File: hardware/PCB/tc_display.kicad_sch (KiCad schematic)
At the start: 41 parts, among them Q1 2N2222, Q2 2N2222, U10 SA15-11SRWA, U11 SA15-11SRWA, U12 SA15-11SRWA, U13 SA15-11SRWA, U14 SA15-11SRWA, U15 SA15-11SRWA, U16 MAX7219, U17 SA15-11SRWA, U18 SA15-11SRWA, U19 SA15-11SRWA, U20 SA15-11SRWA, U3 SA15-11SRWA, U4 SA15-11SRWA, U5 SA15-11SRWA, U6 SA15-11SRWA, U7 MAX7219, U8 SA15-11SRWA, U9 SA15-11SRWA

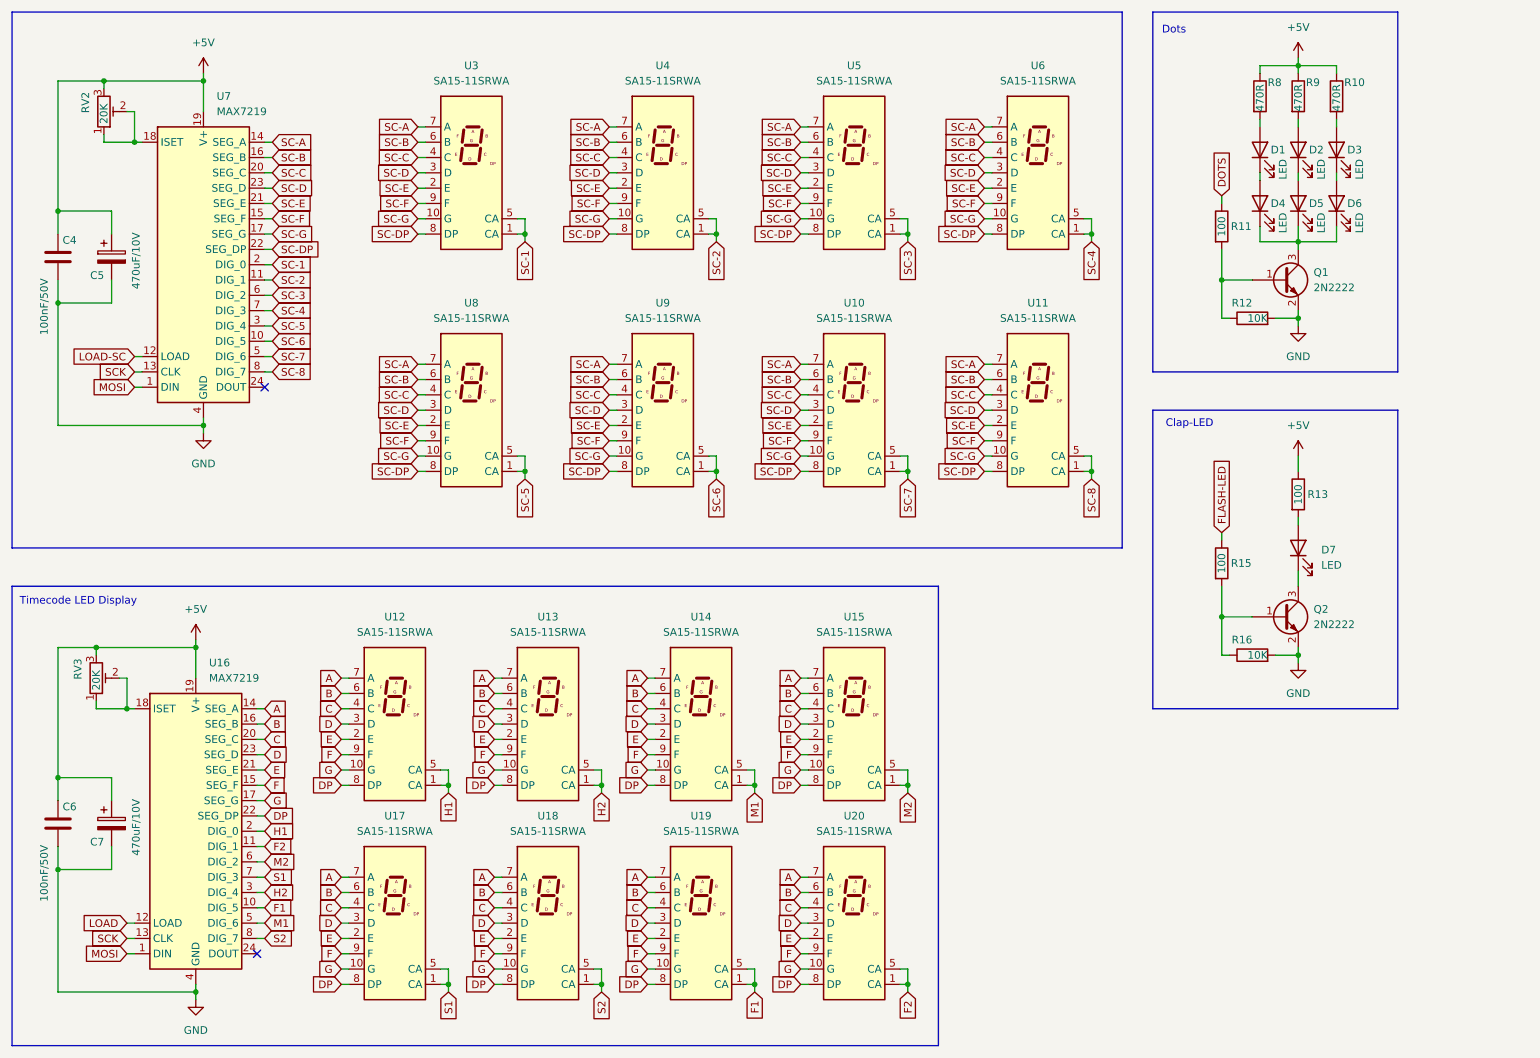
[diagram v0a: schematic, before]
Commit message: dot matrix bugfixes
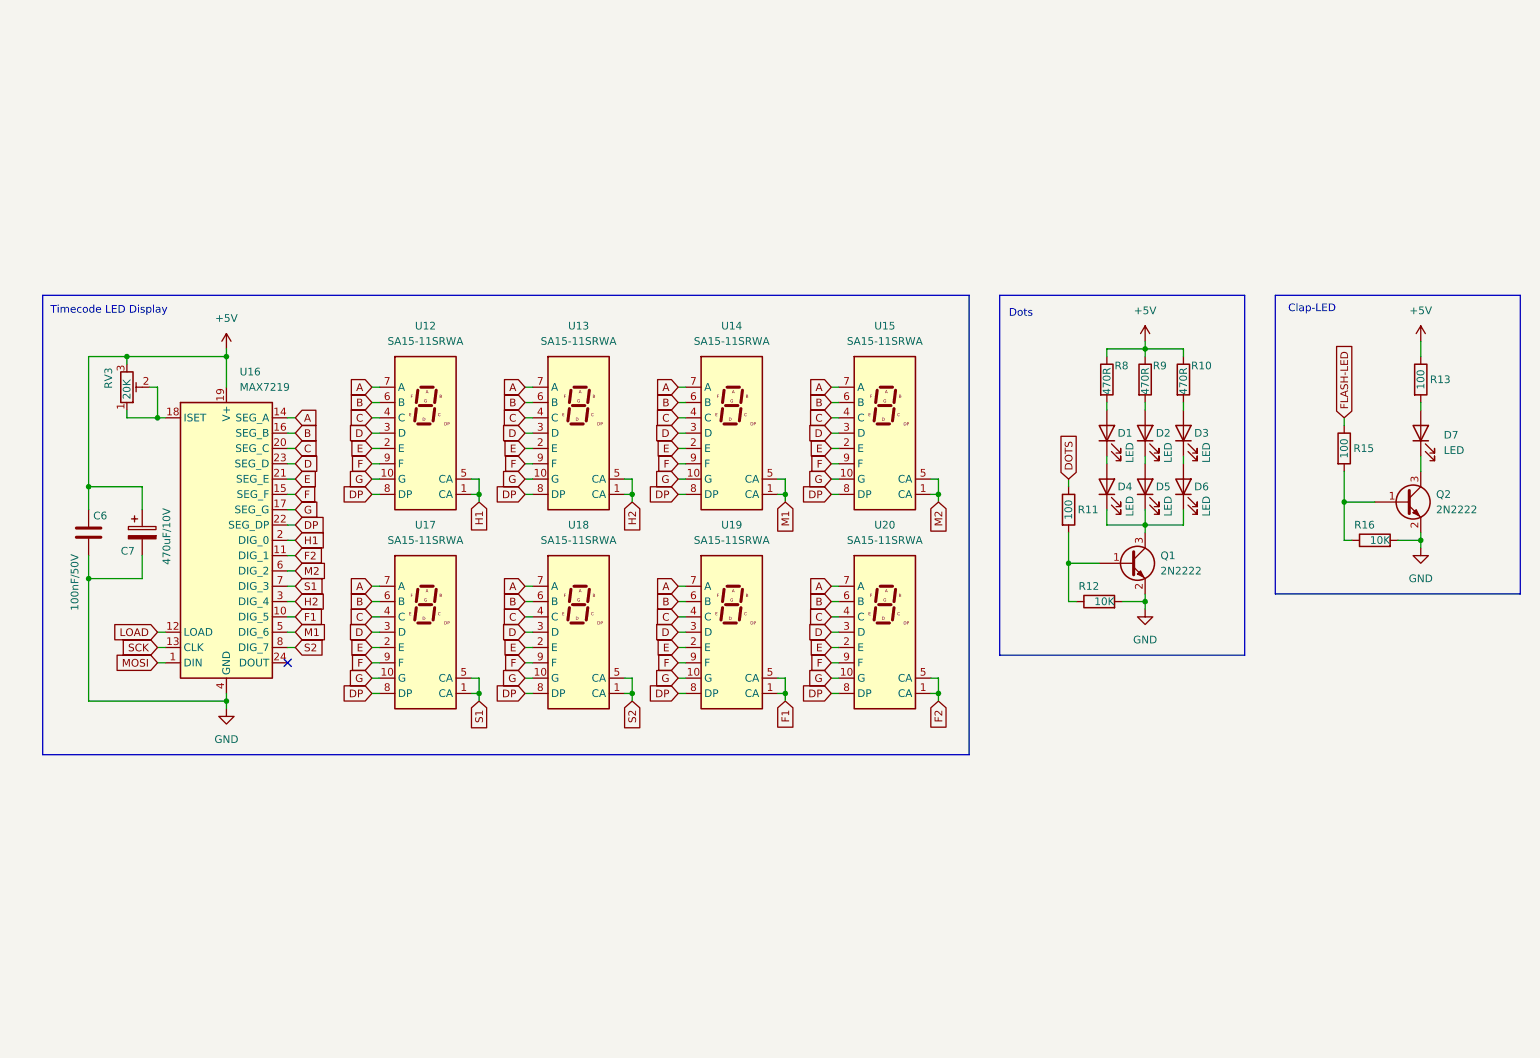
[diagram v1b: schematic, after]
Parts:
- removed C4: 100nF/50V, Capacitor_SMD:C_1206_3216Metric_Pad1.33x1.80mm_HandSolder, symbol Device:C
- removed C5: 470uF/10V, Capacitor_Tantalum_SMD:CP_EIA-7343-31_Kemet-D_Pad2.25x2.55mm_HandSolder, symbol Device:C_Polarized
- removed RV2: 20K, Potentiometer_SMD:Potentiometer_Vishay_TS53YL_Vertical, symbol Device:R_Potentiometer_Trim
- removed U10, U11, U3, U4, U5, U6, U8, U9: SA15-11SRWA, 7-segment-led:FYS-12011A, symbol Display_Character:SA15-11SRWA
- removed U7: MAX7219, Package_SO:SOIC-24W_7.5x15.4mm_P1.27mm, symbol Driver_LED:MAX7219
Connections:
- no-connect marks 2 -> 1
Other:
- moved on the sheet: C6, C7, D1, D2, D3, D4, D5, D6, D7, Q1, Q2, R10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

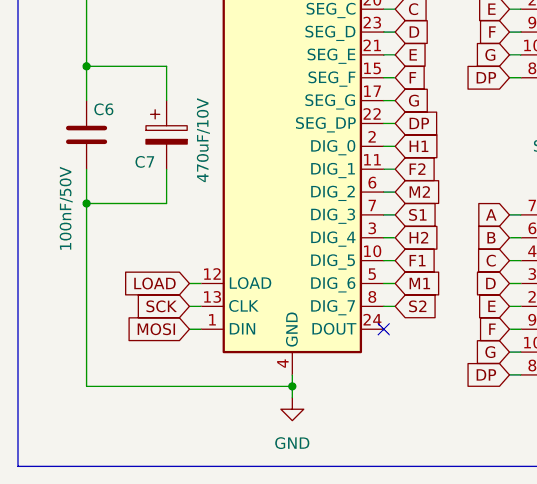
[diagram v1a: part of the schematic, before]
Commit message: added KiCad libraries schematic bugfixes
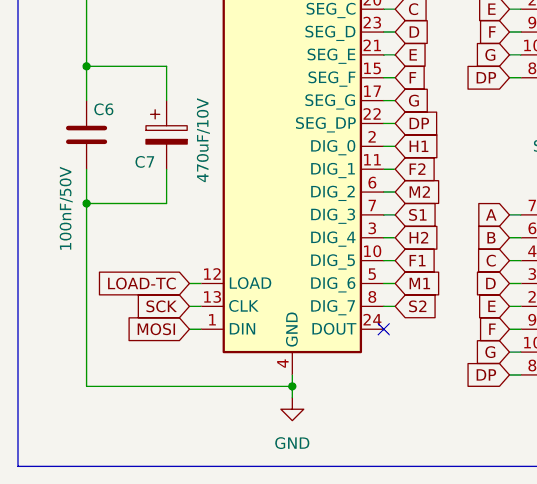
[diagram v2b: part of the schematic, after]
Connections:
- net LOAD renamed LOAD-TC
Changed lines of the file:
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@@
 		)
 	)
-	(global_label "LOAD"
+	(global_label "LOAD-TC"
 		(shape input)
 		(at 44.45 120.65 180)
@@
 		)
 		(property "Intersheetrefs" "${INTERSHEET_REFS}"
-			(at 36.7476 120.65 0)
+			(at 32.9376 120.65 0)
 			(effects
 				(font

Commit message: KiCAD bagfix update
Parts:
- R11: value 100 -> 1k5
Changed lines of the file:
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@@
 			)
 		)
-		(property "Value" "100"
+		(property "Value" "1k5"
 			(at 195.58 100.33 90)
 			(effects

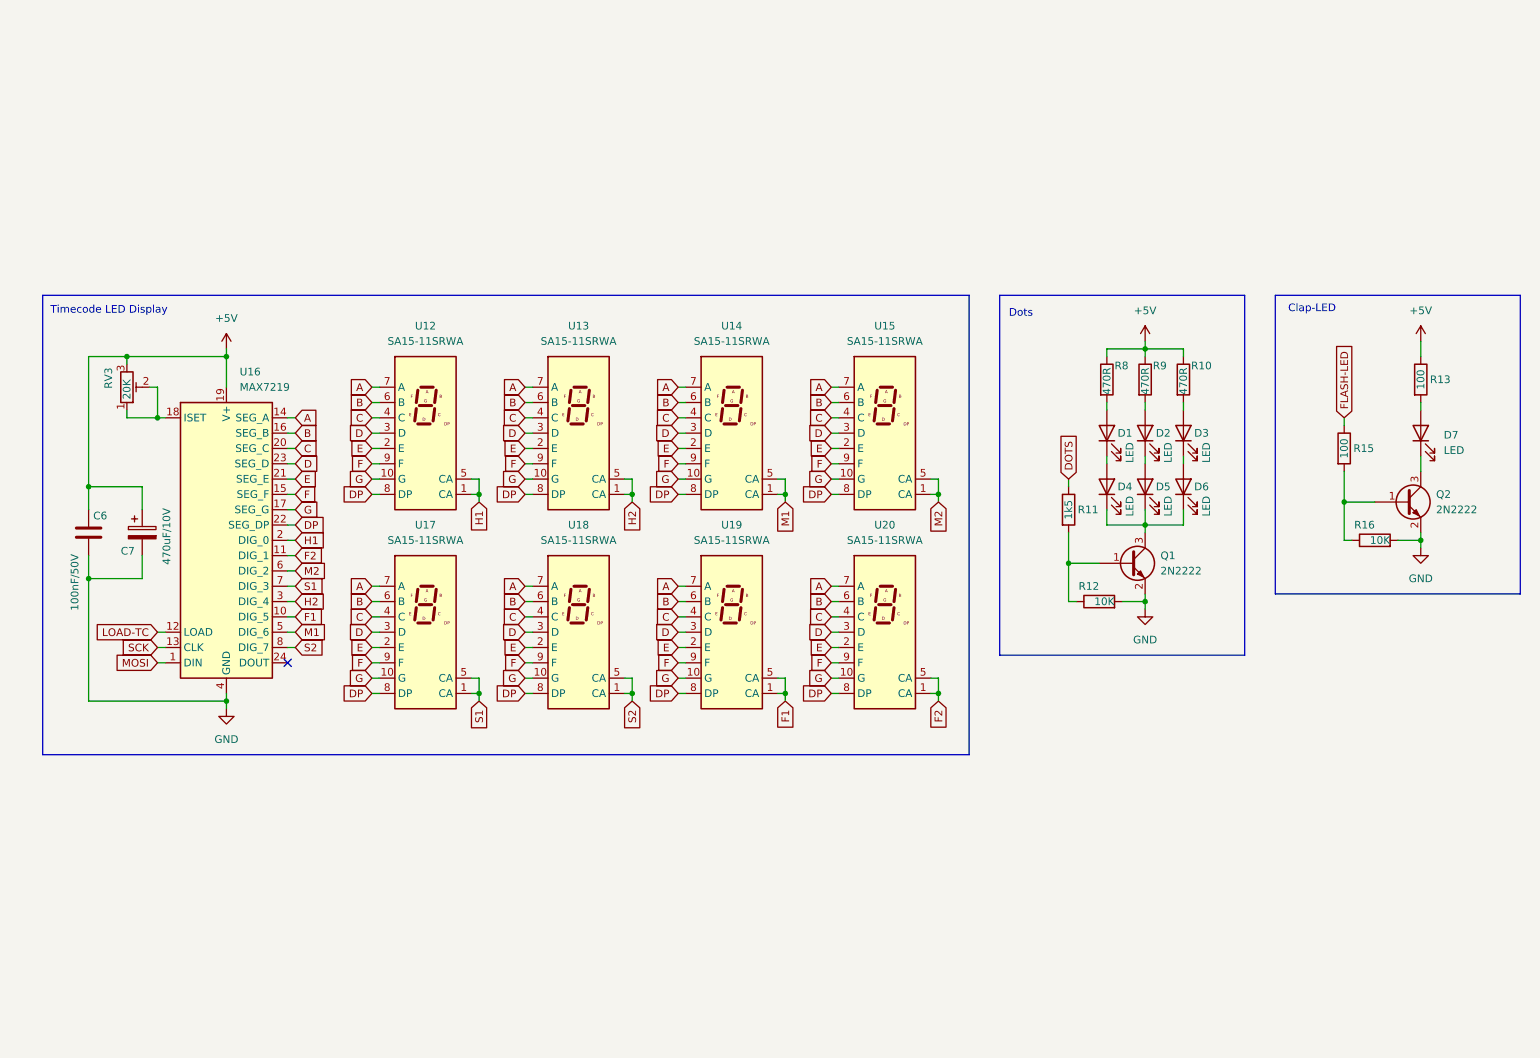
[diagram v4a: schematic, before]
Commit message: level converter added to schematic and pcb
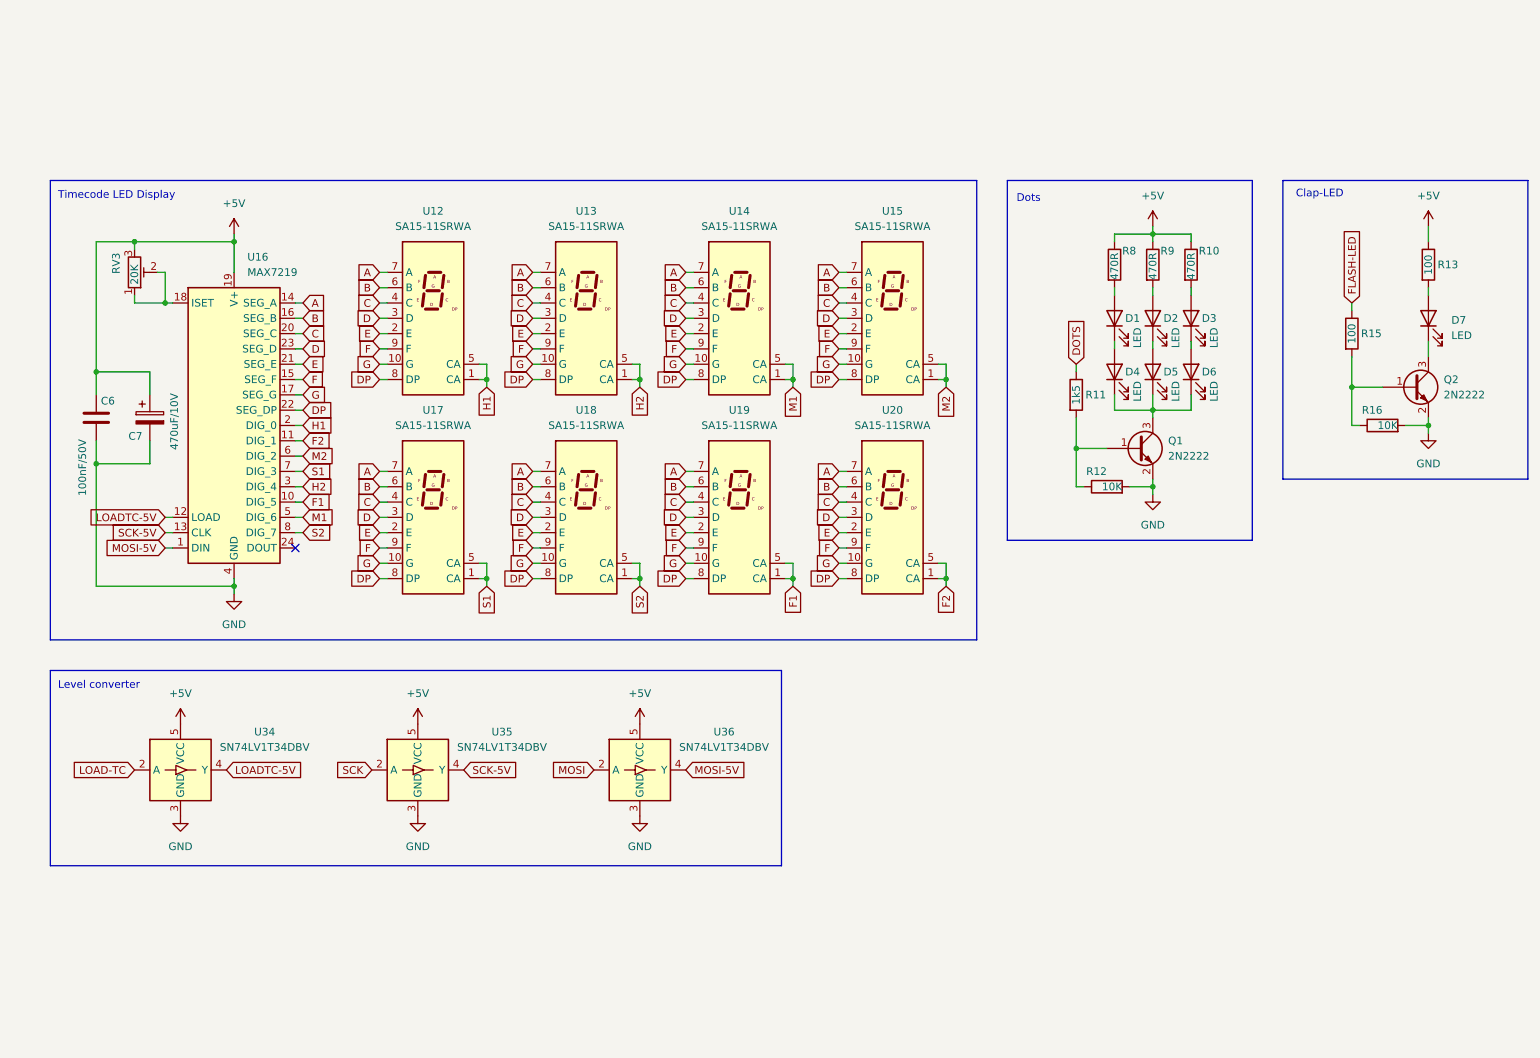
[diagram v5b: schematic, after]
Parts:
- added U34, U35, U36: SN74LV1T34DBV, Package_TO_SOT_SMD:SOT-23-5, symbol Logic_LevelTranslator:SN74LV1T34DBV
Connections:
- net +5V: now also U34.5 (VCC), U35.5 (VCC), U36.5 (VCC)
- net GND: now also U34.3 (GND), U35.3 (GND), U36.3 (GND)
- net LOAD-TC: now also U34.2 (A); no longer U16.12 (LOAD)
- net MOSI: now also U36.2 (A); no longer U16.1 (DIN)
- net SCK: now also U35.2 (A); no longer U16.13 (CLK)
- new net LOADTC-5V: U16.12 (LOAD), U34.4 (Y)
- new net MOSI-5V: U16.1 (DIN), U36.4 (Y)
- new net SCK-5V: U16.13 (CLK), U35.4 (Y)
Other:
- note added: "Level converter"
- moved on the sheet: C6, C7, D1, D2, D3, D4, D5, D6, D7, Q1, Q2, R10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
